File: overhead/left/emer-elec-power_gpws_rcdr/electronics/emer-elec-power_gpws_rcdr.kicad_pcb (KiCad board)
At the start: 2 copper layers, 145 x 133.9 mm, 86 parts, among them J1 Conn_02x01, J2 Conn_02x13_Counter_Clockwise, J3 Conn_02x01, J4 Conn_02x01, J5 Conn_02x01, J6 Conn_02x01

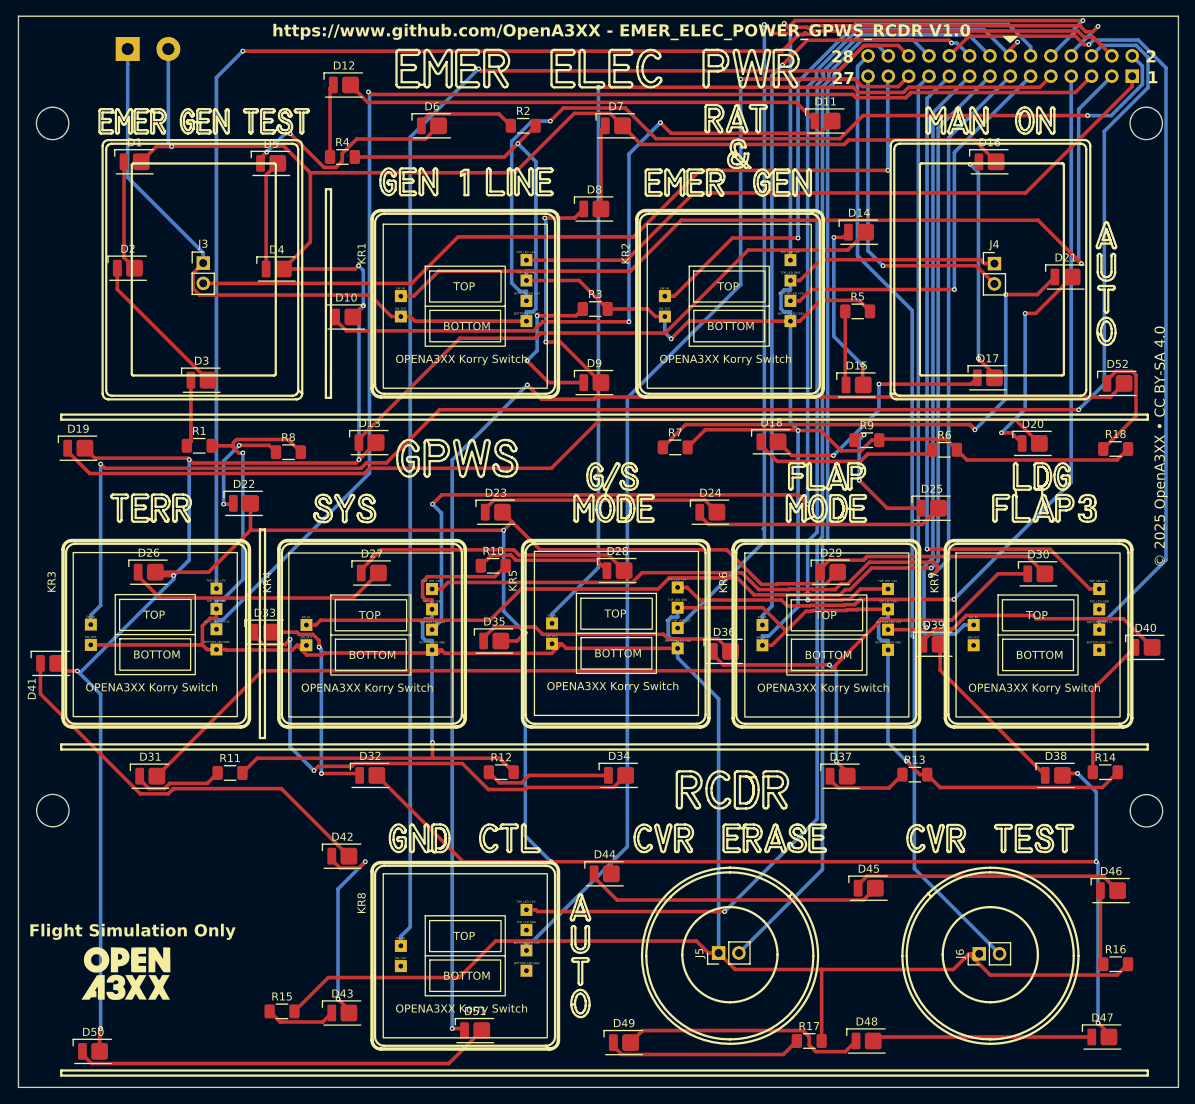
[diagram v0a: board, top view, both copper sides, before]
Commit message: Updated PCB Iteration 2 for Emer Elec Panel
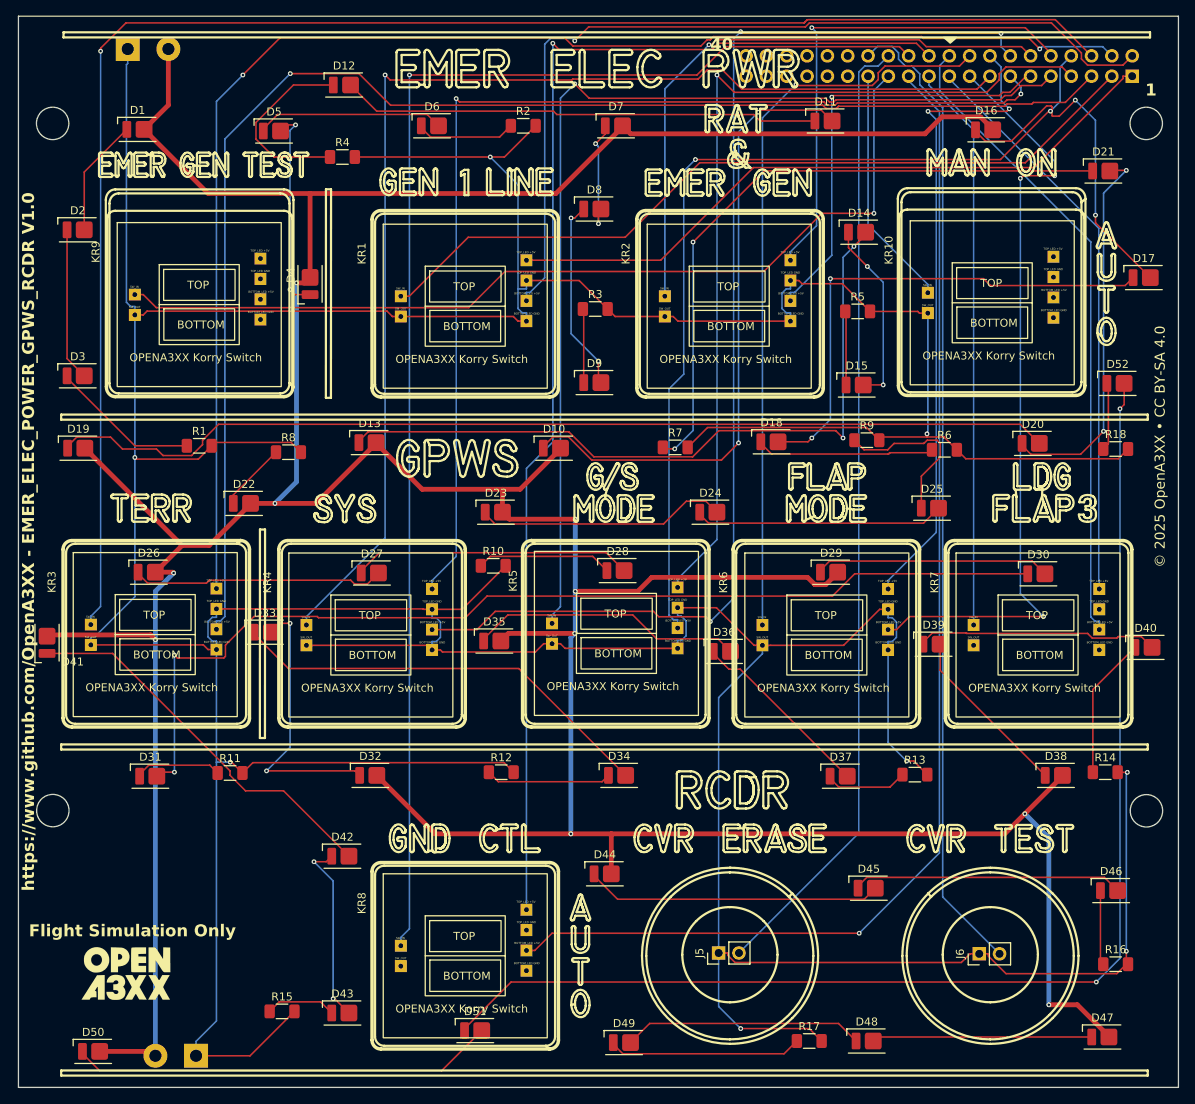
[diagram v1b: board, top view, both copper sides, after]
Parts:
- removed J3, J4: Conn_02x01, Connector_PinHeader_2.54mm:PinHeader_1x02_P2.54mm_Vertical
- added J7: Conn_02x01, TerminalBlock:TerminalBlock_bornier-2_P5.08mm, B.Cu at (96.2, 157.7)
- added KR10: ~, OpenA3XX:Korry Switch, F.Cu at (185.5, 53.3)
- added KR9: ~, OpenA3XX:Korry Switch, F.Cu at (86.3, 53.5)
- J2: value Conn_02x13_Counter_Clockwise -> Conn_02x20_Counter_Clockwise; footprint Connector_PinHeader_2.54mm:PinHeader_2x14_P2.54mm_Vertical -> Connector_PinHeader_2.54mm:PinHeader_2x20_P2.54mm_Vertical
- moved D10 30.7 mm to (140.9, 81.7)
- moved D17 23.2 mm to (214.7, 60.4)
- moved D3 15.5 mm to (81.4, 72.7)
- moved D21 14.1 mm to (209.6, 47.0)
- moved D2 7.91 mm to (81.4, 54.4)
- moved D4 4.55 mm to (110.5, 61.2), turned to 90 degrees
- moved D5 4.07 mm to (106.0, 42.0)
- moved D1 4.07 mm to (88.9, 41.9)
- moved D16 4.02 mm to (195.0, 41.9)
- moved D41 2.64 mm to (77.6, 106.0), turned to 90 degrees
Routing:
- net Net-(D17-K): track 31.5 -> 63.9 mm
- net Net-(J2-Pin_20): track 104.4 -> 80.8 mm, vias 1 -> 0
- net Net-(J2-Pin_17): track 76.4 -> 97.3 mm, vias 1 -> 3
- net Net-(D20-K): track 27.0 -> 48.0 mm
- net Net-(J2-Pin_16): track 101.4 -> 80.5 mm, vias 1 -> 2
- net +12V: track 579.0 -> 558.6 mm, vias 14 -> 10
- net Net-(J2-Pin_3): track 116.6 -> 100.3 mm, vias 1 -> 0
- net Net-(D13-K): track 74.9 -> 91.1 mm, vias 0 -> 2
- net Net-(D12-K): track 9.17 -> 23.9 mm
- net Net-(D21-K): track 67.8 -> 82.0 mm
- net Net-(D16-K): track 29.2 -> 43.1 mm
- net Net-(J2-Pin_8): track 128.5 -> 115.6 mm
- net Net-(J2-Pin_23): track 142.4 -> 155.4 mm
- net Net-(J2-Pin_25): track 103.2 -> 115.8 mm
- net Net-(D4-K): track 13.8 -> 25.8 mm, vias 0 -> 2
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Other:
- board text added: "1-GEN1-TOP_LED 2-GEN1-BOTTOM_LED 3-GEN1-KORRY_SW 4-RAT & EMER GEN-TOP_LED 5-RAT & EMER GEN-BOTTOM_LED 6-RAT & EMER GEN-KORRY_SW 7-TERR-TOP_LED 8-TERR-BOTTOM_LED 9-TERR-KORRY_SW 10-G/S Mode-TOP_LED 11-G/S Mode-BOTTOM_LED 12-G/S Mode-KORRY_SW 13-Flap Mode-TOP_LED 14-Flap Mode-BOTTOM_LED 15-Flap Mode-KORRY_SW 16-LDG Flap 3-TOP_LED 17-LDG Flap 3-BOTTOM_LED 18-LDG Flap 3-KORRY_SW 19-SYS-TOP_LED 20-SYS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"
- board text added: "40"
- board text removed: "2"
- board text removed: "27"
- board text removed: "28"
